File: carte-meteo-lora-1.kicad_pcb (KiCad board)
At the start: 2 copper layers, 118 parts, among them J1 TC2030, J2 Conn_01x04, J3 Conn_01x04, J4 Conn_Coaxial, J5 USB_C_Receptacle_USB2.0_14P, J6 Solar_Cell, J7 Conn_01x02, J8 Battery_Cell, Q1 AO4882, Q2 AO4882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

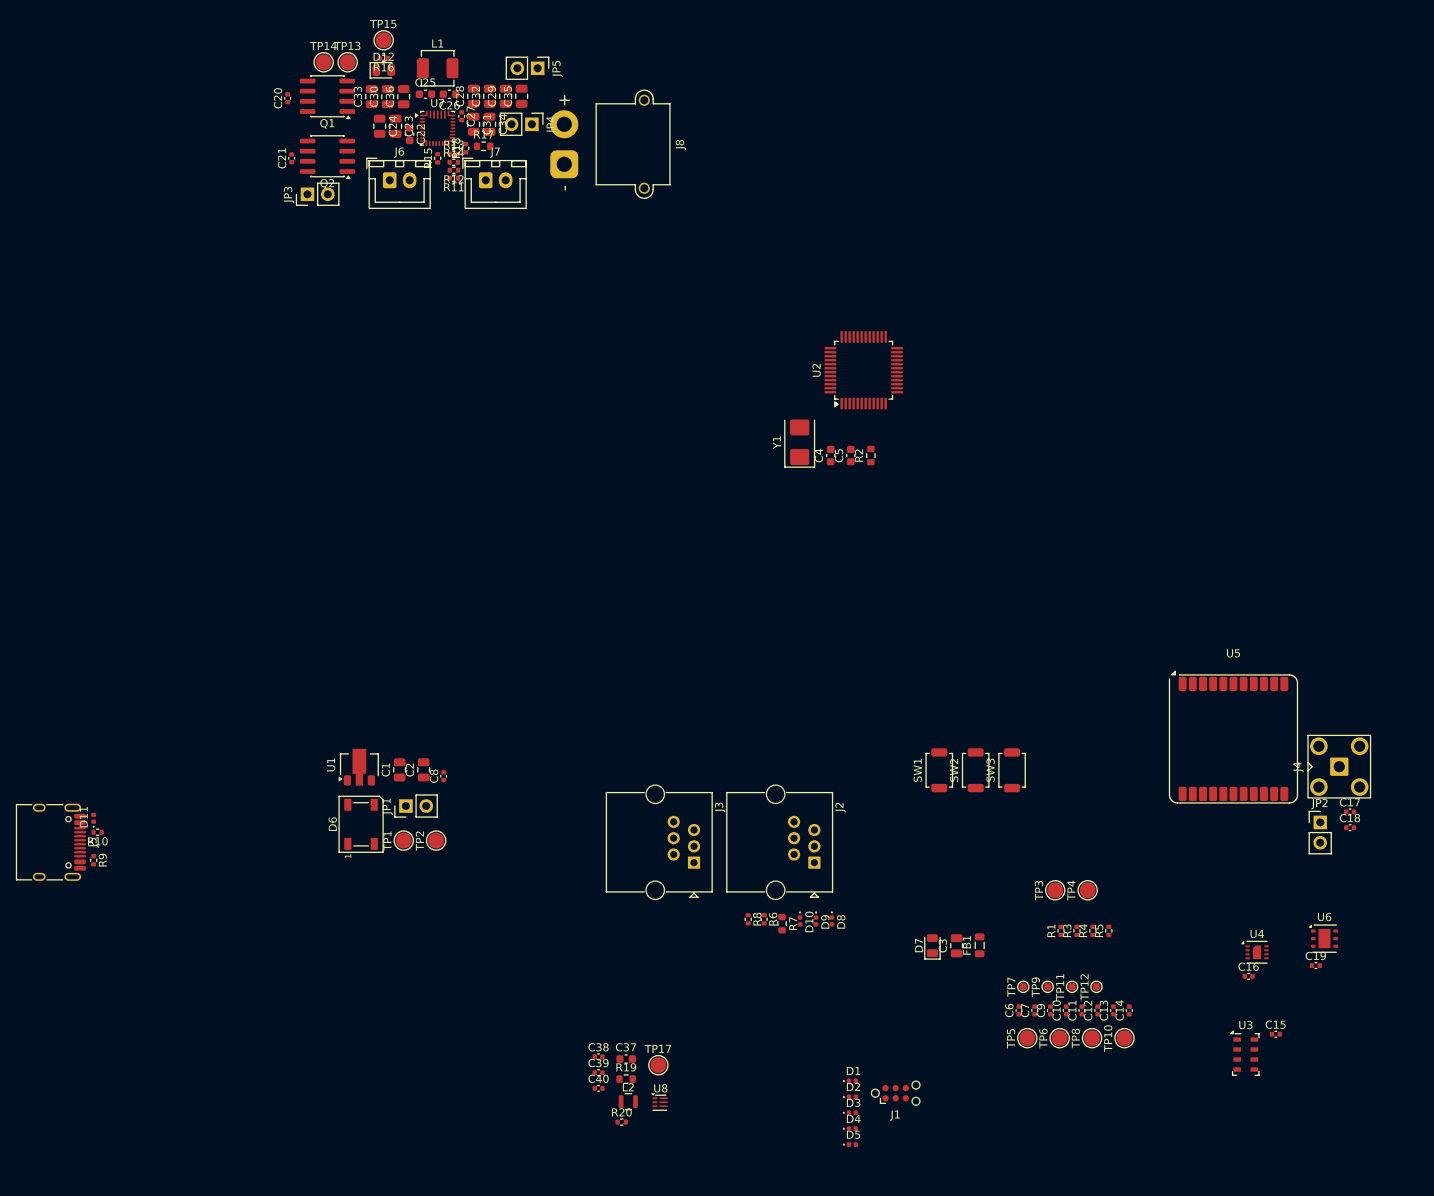
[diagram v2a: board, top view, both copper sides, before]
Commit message: pcb: add rgb led routing
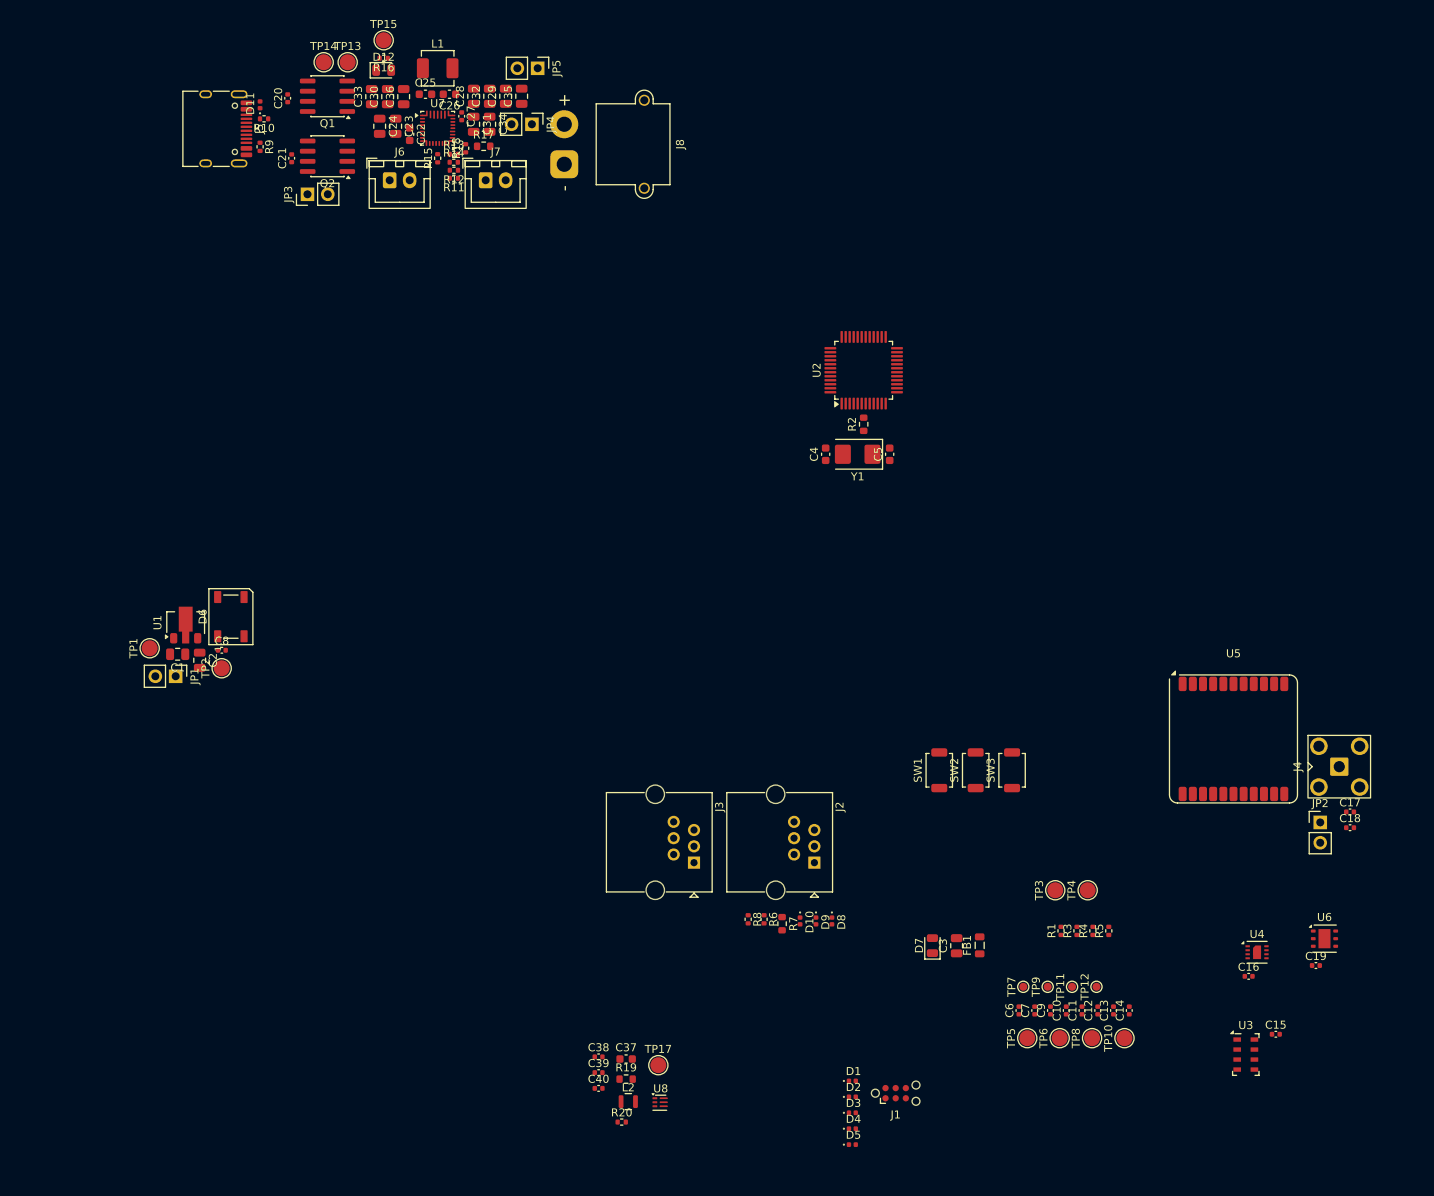
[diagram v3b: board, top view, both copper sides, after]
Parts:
- moved D11 91.6 mm to (62.5, 35.8)
- moved J5 91.6 mm to (56.8, 38.8)
- moved R10 91.6 mm to (63.0, 37.6)
- moved R9 91.6 mm to (62.5, 41.1)
- moved TP1 39.8 mm to (48.8, 103.8)
- moved TP2 34.4 mm to (57.8, 106.2)
- moved JP1 33.0 mm to (52.0, 107.2), turned to -90 degrees
- moved C8 31.9 mm to (57.8, 104.0), turned to 0 degrees
- moved C1 31.3 mm to (52.2, 104.5), turned to 180 degrees
- moved C2 31.2 mm to (55.0, 105.2), turned to -90 degrees
- moved D6 30.6 mm to (58.9, 99.8)
- moved U1 28.1 mm to (53.2, 100.5)
- moved Y1 7.40 mm to (137.2, 79.5), turned to 180 degrees
- moved C5 4.86 mm to (141.2, 79.5)
- moved R2 4.02 mm to (138.0, 75.8)
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
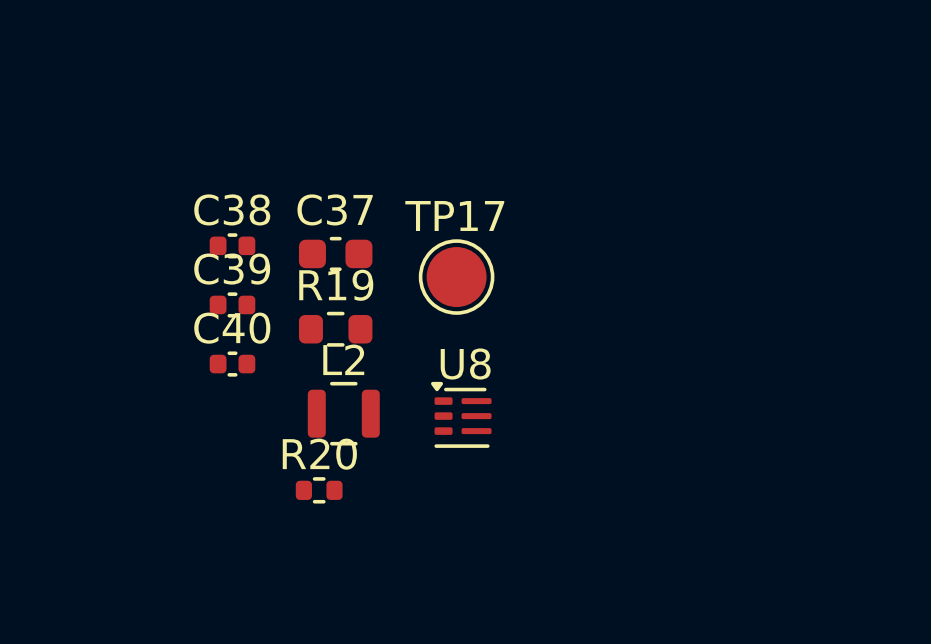
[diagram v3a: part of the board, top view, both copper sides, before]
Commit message: pcb: add smps routing
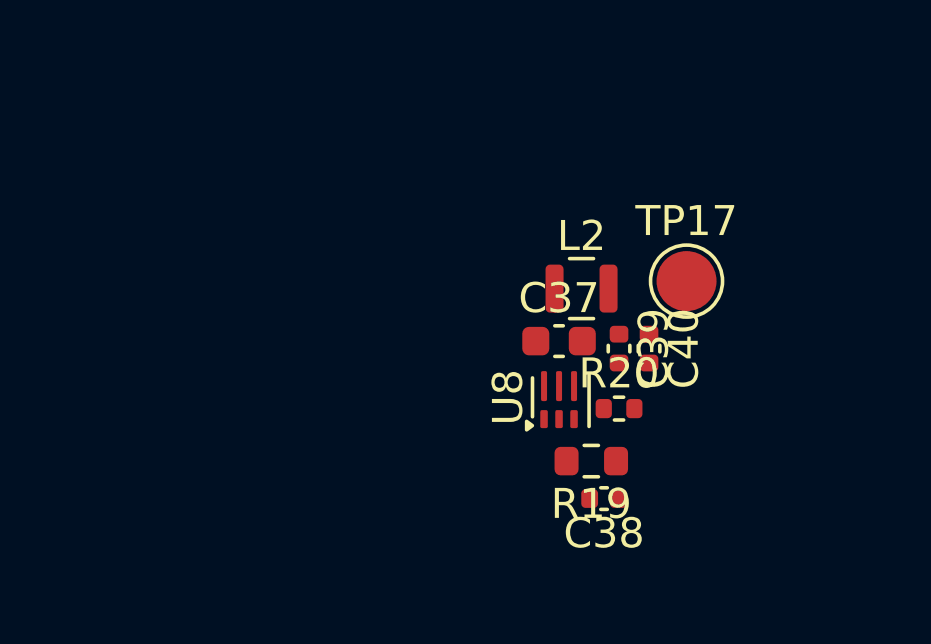
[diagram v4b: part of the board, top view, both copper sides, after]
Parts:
- moved C38 15.0 mm to (117.2, 163.2), turned to 180 degrees
- moved C40 13.9 mm to (118.8, 158.2), turned to -90 degrees
- moved C39 13.0 mm to (117.8, 158.2), turned to -90 degrees
- moved R20 10.4 mm to (117.8, 160.2)
- moved R19 9.59 mm to (116.8, 162.0), turned to 180 degrees
- moved L2 8.96 mm to (116.5, 156.2)
- moved C37 7.99 mm to (115.8, 158.0)
- moved TP17 7.67 mm to (120.0, 156.0)
- moved U8 3.49 mm to (116.0, 159.9), turned to 90 degrees

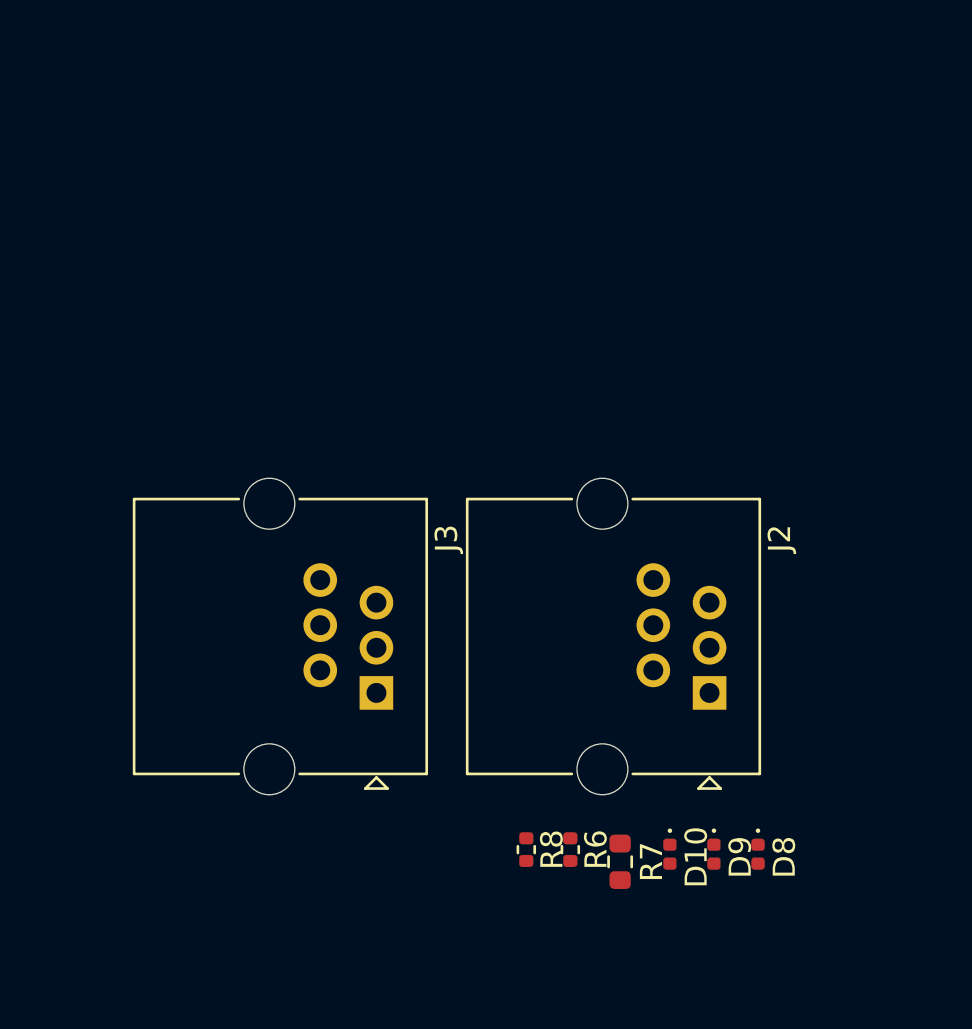
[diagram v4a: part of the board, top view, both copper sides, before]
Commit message: pcb: add wind/rain connectors layout
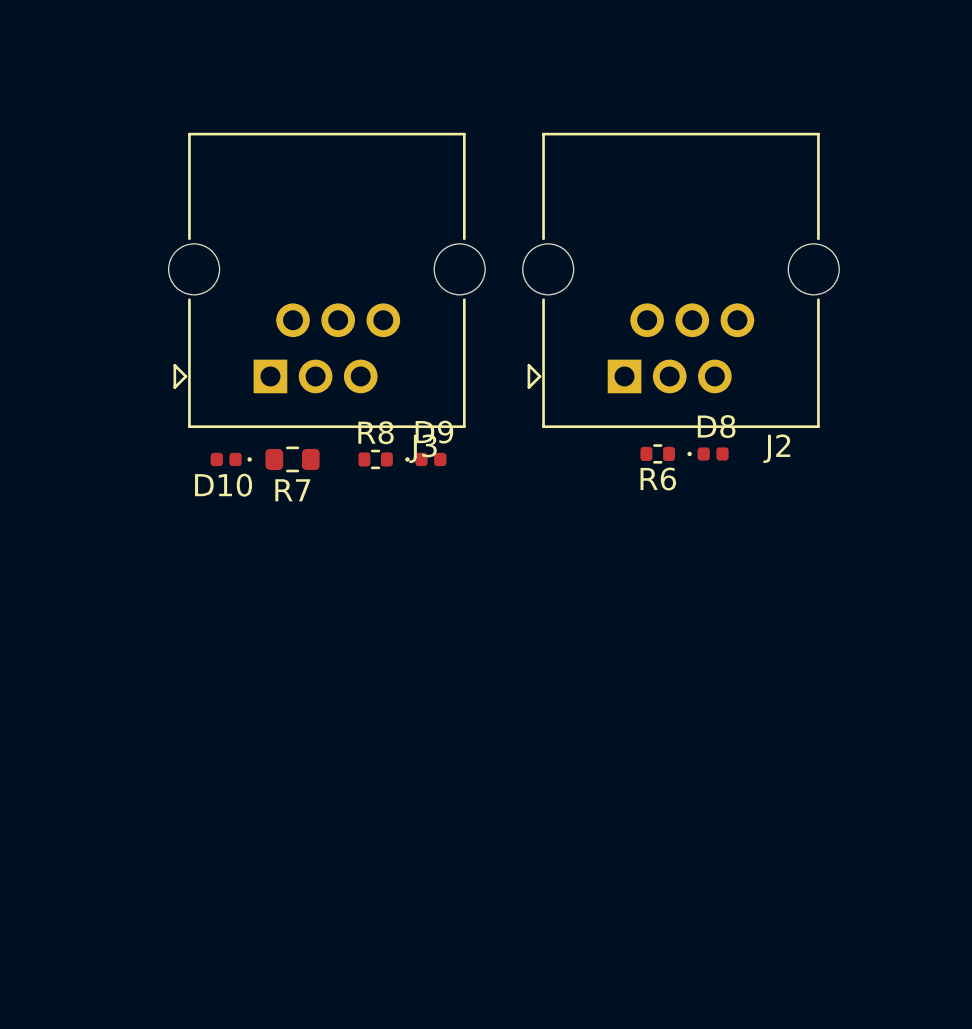
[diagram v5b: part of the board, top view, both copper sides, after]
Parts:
- moved D10 26.8 mm to (110.0, 120.0), turned to 180 degrees
- moved R7 23.4 mm to (113.0, 120.0), turned to 180 degrees
- moved D9 21.9 mm to (119.2, 120.0), turned to 0 degrees
- moved R8 18.9 mm to (116.8, 120.0), turned to 0 degrees
- moved R6 18.3 mm to (129.5, 119.8), turned to 180 degrees
- moved D8 18.2 mm to (132.0, 119.8), turned to 0 degrees
- moved J3 15.1 mm to (112.0, 116.2), turned to 180 degrees
- moved J2 14.8 mm to (128.0, 116.2), turned to 180 degrees

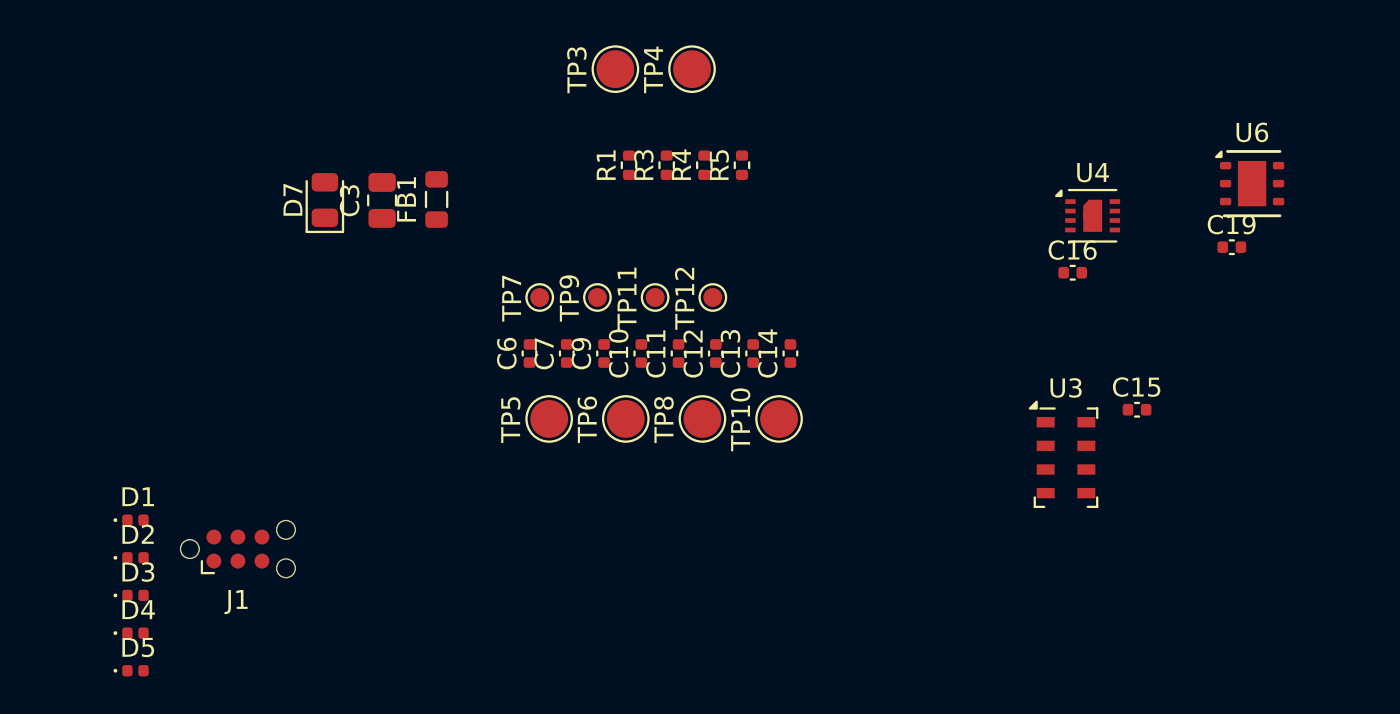
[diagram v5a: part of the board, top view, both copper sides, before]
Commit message: pcb: add sensors layout
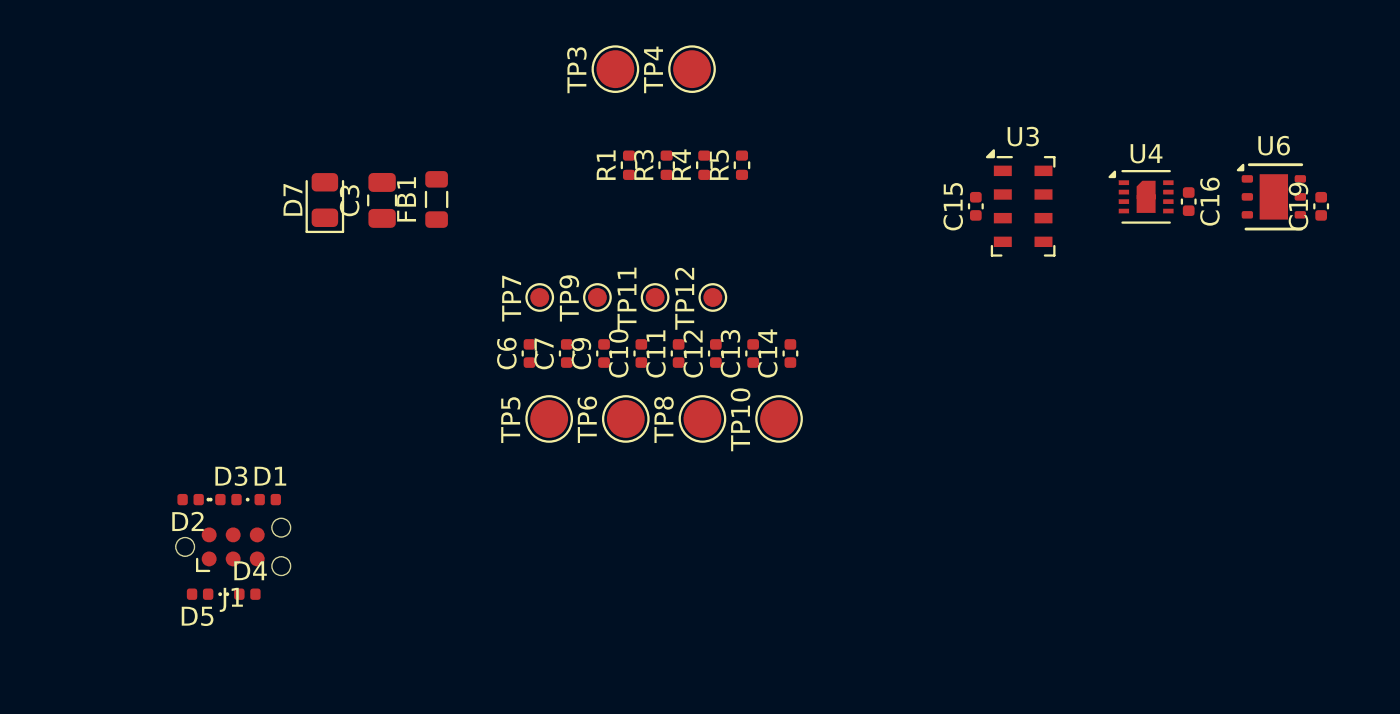
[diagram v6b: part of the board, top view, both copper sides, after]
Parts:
- moved C15 13.7 mm to (181.0, 141.2), turned to 90 degrees
- moved U3 13.5 mm to (183.5, 141.2)
- moved C16 7.19 mm to (192.2, 141.0), turned to -90 degrees
- moved D1 7.07 mm to (143.6, 156.8)
- moved D3 7.06 mm to (141.5, 156.8)
- moved D4 6.26 mm to (142.5, 161.8)
- moved D5 5.29 mm to (140.0, 161.8), turned to 180 degrees
- moved C19 5.19 mm to (199.2, 141.2), turned to 90 degrees
- moved D2 4.24 mm to (139.5, 156.8), turned to 180 degrees
- moved U4 3.00 mm to (190.0, 140.8)
- moved U6 1.35 mm to (196.8, 140.8)
- moved J1 0.28 mm to (141.8, 159.2)
